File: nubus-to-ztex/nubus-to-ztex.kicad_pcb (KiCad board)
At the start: 4 copper layers, 161.6 x 100 mm, 101 parts, among them J1 87831-1420 (2x7 M 2mm), J2 47219-2001 (micro-sd), J3 Conn_01x06_Male, J4 85003-0567 (DIN 41612C 3x32 p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, J5 10029449-111RLF (HDMI A), J6 105017-0001 (USB micro-B), J7 640456-3 (Fan), J8 A2541HWR-2x8P (Pmod 2x8 F), U1 74LVT125PW,118, U10 SN65220DBV, U11 TPS2051CDBV, U13 SN74CB3T3245PWR, U14 SN74CB3T3245PWR, U15 SN74CB3T3245PWR, U2 74LVT125PW,118, U3 74LVT125PW,118, U5 74LVT245BPW,118, U6 74LVT245BPW,118, U7 74LVT245BPW,118, U8 74LVT245BPW,118, U9 TPD12S016PWR, X1 ASE-xxxMHz

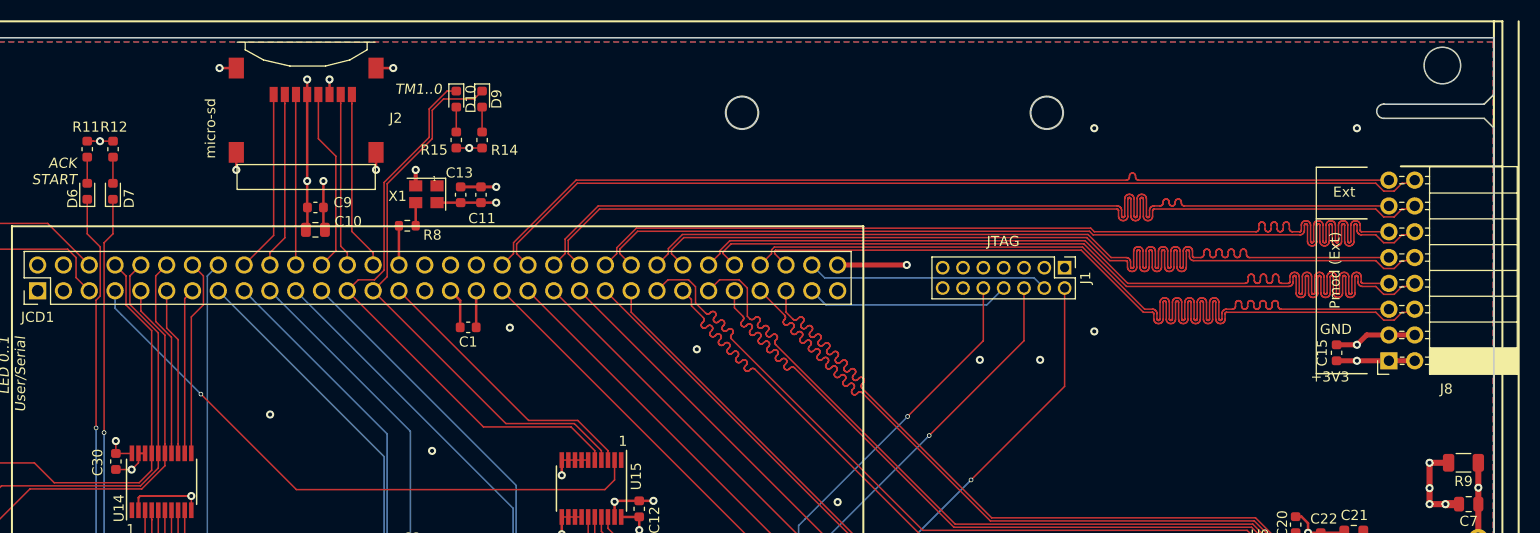
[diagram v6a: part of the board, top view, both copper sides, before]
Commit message: more JLCPCB BoM optimization
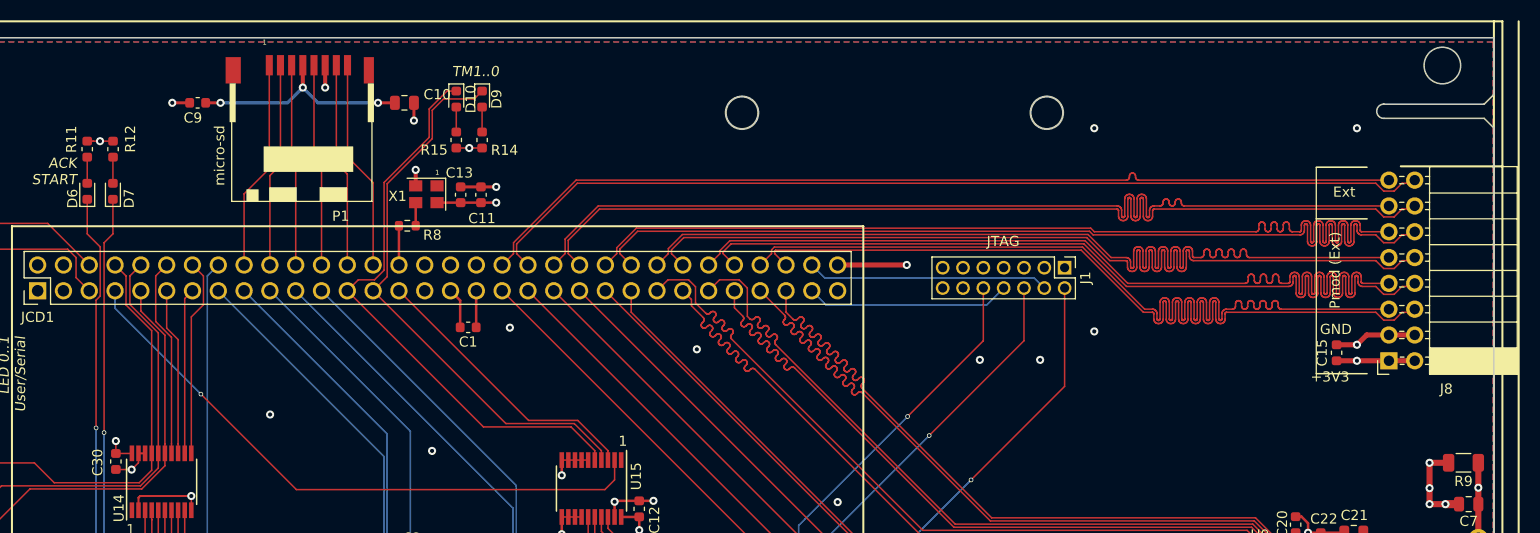
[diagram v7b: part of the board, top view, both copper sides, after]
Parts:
- removed J2: 47219-2001 (micro-sd), MOLEX_47219-2001:MOLEX_47219-2001
- added P1: DM3CS-SF, For_SeeedStudio:HRS_DM3CS-SF, F.Cu at (156.0, 14.0)
- moved C9 15.5 mm to (145.8, 11.5), turned to 180 degrees
- moved C10 15.3 mm to (166.1, 11.5)
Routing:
- net GND: track 1490.1 -> 1464.1 mm, vias 88 -> 85
- net SD_D0: track 17.0 -> 20.1 mm
- net SD_D1: track 17.6 -> 20.7 mm
- net SD_CMD: track 16.8 -> 19.8 mm
- net SD_D2: track 18.0 -> 20.7 mm
- net SD_D3: track 17.4 -> 20.1 mm
- net SD_CLK: track 18.1 -> 20.0 mm
- net +3V3: track 627.9 -> 628.2 mm, vias 30 -> 31

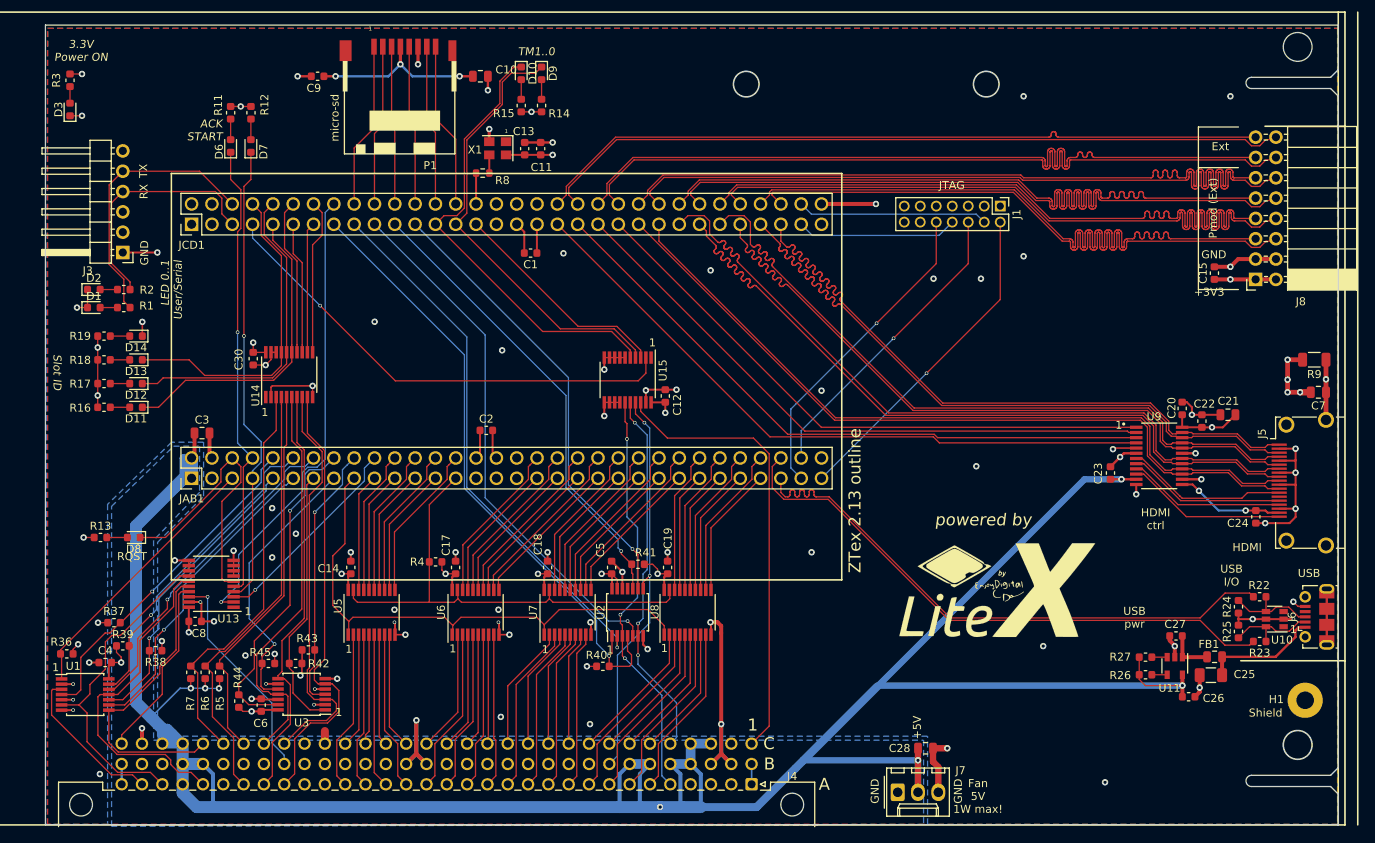
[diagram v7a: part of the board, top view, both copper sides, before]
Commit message: even more JLCPCB BoM optimization
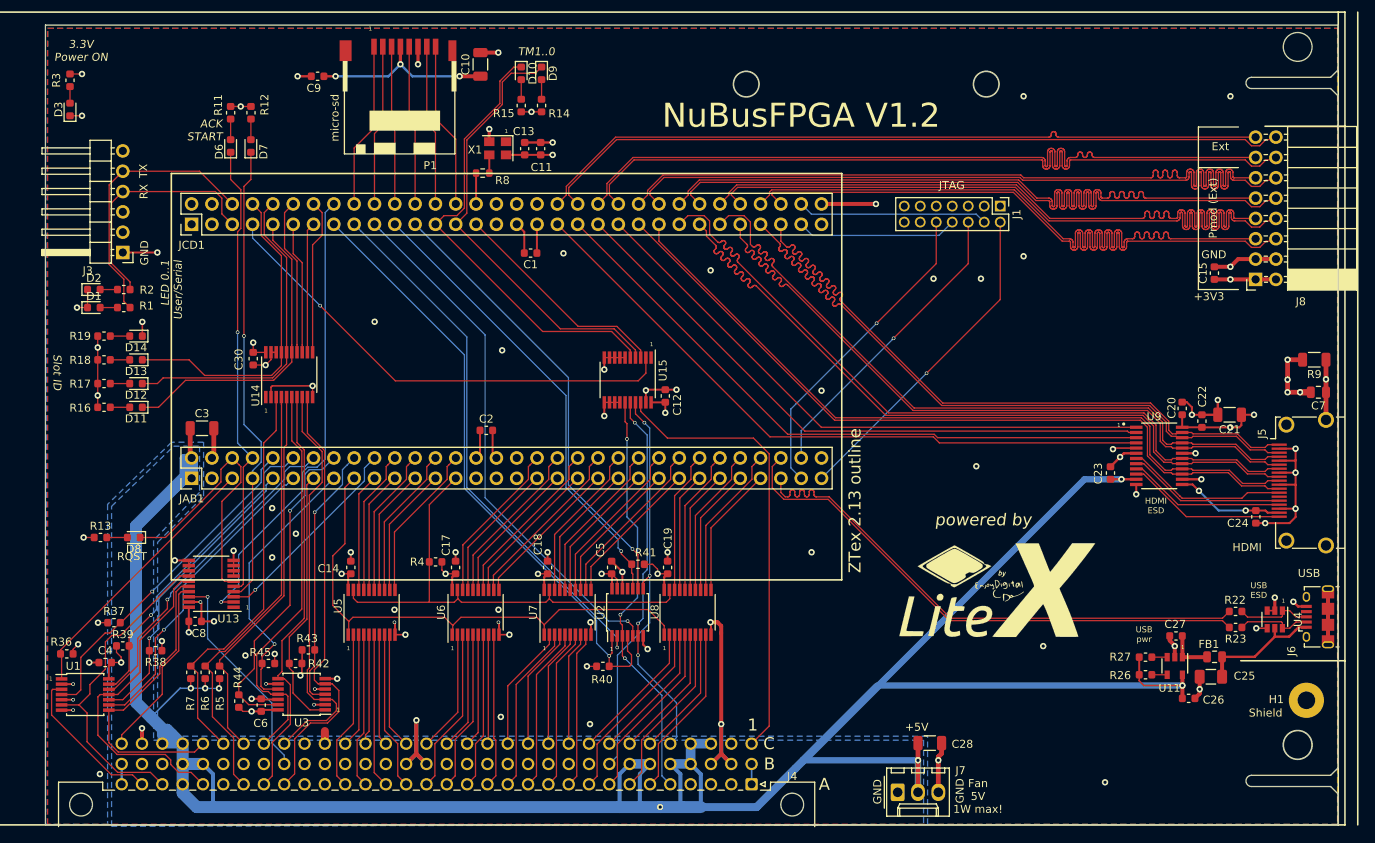
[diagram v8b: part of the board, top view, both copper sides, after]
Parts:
- removed R24, R25: 15k, Resistor_SMD:R_0603_1608Metric
- removed U10: SN65220DBV, Package_TO_SOT_SMD:SOT-23-6
- added U4: SRV05-4, Package_TO_SOT_SMD:SOT-23-6, F.Cu at (265.4, 79.4)
- C10, C21, C28, C3: value 47uF 10V 0805 -> 47uF 10V 1206; footprint Capacitor_SMD:C_0805_2012Metric -> Capacitor_SMD:C_1206_3216Metric
- J6: value 105017-0001 (USB micro-B) -> 10118194-0001LF (USB micro-B); footprint Connector_USB:USB_Micro-B_Molex-105017-0001 -> Connector_USB:USB_Micro-B_Amphenol_10118194_Horizontal
- U1, U2, U3: value 74LVT125PW,118 -> SN74LVTH125PWR
- moved R22 3.53 mm to (260.5, 78.4)
- moved R23 3.48 mm to (260.5, 80.4)
- moved C10 1.48 mm to (166.1, 10.0), turned to 90 degrees
- moved C28 0.84 mm to (222.3, 94.8)
- moved C3 0.60 mm to (131.3, 55.5)
- moved C21 0.21 mm to (259.8, 53.8)
- moved C25 0.20 mm to (257.4, 86.6)
- moved C26 0.20 mm to (254.6, 89.3)
- moved J6 0.09 mm to (270.8, 79.1)
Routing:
- net GND: track 1464.1 -> 1444.8 mm, vias 85 -> 86
- net USBH0_D+: track 72.7 -> 68.5 mm
- net USBH0_D-: track 72.7 -> 68.5 mm
- net /usb/USB_D-: track 12.4 -> 9.41 mm
- net /usb/USB_D+: track 12.0 -> 9.41 mm
- net SHIELD: track 71.1 -> 69.6 mm
- net +3V3: track 628.2 -> 626.8 mm, vias 31 -> 32
- net +5V: track 337.0 -> 338.3 mm
- net /usb/VBus_USB0: track 14.7 -> 15.6 mm
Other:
- board text added: "HDMI ESD"
- board text added: "NuBusFPGA V1.2"
- board text added: "USB ESD"
- board text removed: "HDMI ctrl"
- board text removed: "USB I/O"
